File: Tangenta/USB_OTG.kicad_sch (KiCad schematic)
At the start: 21 parts, among them J11 TYPEC-304-ACP16, U10 TUSB321RWBR, U11 AOZ1353DI-01, U12 PUSB2X4Y-N, U9 PUSB2X4Y-N

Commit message: ...
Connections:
- net GNDREF: now also J11.A1B12 (GND), J11.B1A12 (GND); no longer J11.A1_B12 (GND), J11.B1_A12 (GND)
- net USB_DR.VBUS: now also J11.A4B9 (VBUS), J11.B4A9 (VBUS); no longer J11.A4_B9 (VBUS), J11.B4_A9 (VBUS)
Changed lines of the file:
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@@
     (stroke (width 0) (type default))
   )
-  (wire (pts (xy 102.108 142.494) (xy 86.36 142.494))
+  (wire (pts (xy 99.568 142.494) (xy 83.82 142.494))
     (stroke (width 0) (type default))
   )
@@
     (stroke (width 0) (type default))
   )
-  (wire (pts (xy 124.968 150.114) (xy 140.716 150.114))
+  (wire (pts (xy 127.508 150.114) (xy 143.256 150.114))
     (stroke (width 0) (type default))
   )
@@
     (stroke (width 0) (type default))
   )
-  (wire (pts (xy 102.108 145.034) (xy 86.36 145.034))
+  (wire (pts (xy 99.568 145.034) (xy 83.82 145.034))
     (stroke (width 0) (type default))
   )
@@
     (stroke (width 0) (type default))
   )
-  (wire (pts (xy 124.968 152.654) (xy 140.716 152.654))
+  (wire (pts (xy 127.508 152.654) (xy 143.256 152.654))
     (stroke (width 0) (type default))
   )
@@
     (stroke (width 0) (type default))
   )
-  (wire (pts (xy 102.108 152.654) (xy 86.36 152.654))
+  (wire (pts (xy 99.568 152.654) (xy 83.82 152.654))
     (stroke (width 0) (type default))
   )
@@
     (stroke (width 0) (type default))
   )
-  (wire (pts (xy 124.968 139.954) (xy 140.716 139.954))
+  (wire (pts (xy 127.508 139.954) (xy 143.256 139.954))
     (stroke (width 0) (type default))
   )
@@
     (stroke (width 0) (type default))
   )
-  (wire (pts (xy 124.968 145.034) (xy 140.716 145.034))
+  (wire (pts (xy 127.508 145.034) (xy 143.256 145.034))
     (stroke (width 0) (type default))
   )
@@
     (stroke (width 0) (type default))
   )
-  (wire (pts (xy 86.36 150.114) (xy 102.108 150.114))
+  (wire (pts (xy 83.82 150.114) (xy 99.568 150.114))
     (stroke (width 0) (type default))
   )
@@
     (stroke (width 0) (type default))
   )
-  (wire (pts (xy 102.108 147.574) (xy 86.36 147.574))
+  (wire (pts (xy 99.568 147.574) (xy 83.82 147.574))
     (stroke (width 0) (type default))
   )
@@
     (stroke (width 0) (type default))
   )
-  (wire (pts (xy 124.968 147.574) (xy 140.716 147.574))
+  (wire (pts (xy 127.508 147.574) (xy 143.256 147.574))
     (stroke (width 0) (type default))
   )
@@
     (effects (font (size 1.27 1.27)) (justify right bottom))
   )
-  (label "USB_DR.P" (at 86.36 145.034 0) (fields_autoplaced)
+  (label "USB_DR.P" (at 83.82 145.034 0) (fields_autoplaced)
     (effects (font (size 1.27 1.27)) (justify left bottom))
   )
@@
     (effects (font (size 1.27 1.27)) (justify left bottom))
   )
-  (label "USB_DR.N" (at 86.36 142.494 0) (fields_autoplaced)
+  (label "USB_DR.N" (at 83.82 142.494 0) (fields_autoplaced)
     (effects (font (size 1.27 1.27)) (justify left bottom))
   )
@@
     (effects (font (size 1.27 1.27)) (justify left bottom))
   )
-  (label "USB_DR.N" (at 140.716 145.034 180) (fields_autoplaced)
-    (effects (font (size 1.27 1.27)) (justify right bottom))
-  )
-  (label "GND" (at 86.36 152.654 0) (fields_autoplaced)
+  (label "USB_DR.N" (at 143.256 145.034 180) (fields_autoplaced)
+    (effects (font (size 1.27 1.27)) (justify right bottom))
+  )
+  (label "GND" (at 83.82 152.654 0) (fields_autoplaced)
     (effects (font (size 1.27 1.27)) (justify left bottom))
   )
@@
     (effects (font (size 1.27 1.27)) (justify left bottom))
   )
-  (label "USB_DR_CC2" (at 140.716 150.114 180) (fields_autoplaced)
+  (label "USB_DR_CC2" (at 143.256 150.114 180) (fields_autoplaced)
     (effects (font (size 1.27 1.27)) (justify right bottom))
   )
@@
     (effects (font (size 1.27 1.27)) (justify right bottom))
   )
-  (label "USB_DR.VBUS" (at 86.36 150.114 0) (fields_autoplaced)
+  (label "USB_DR.VBUS" (at 83.82 150.114 0) (fields_autoplaced)
     (effects (font (size 1.27 1.27)) (justify left bottom))
   )
@@
     (effects (font (size 1.27 1.27)) (justify right bottom))
   )
-  (label "USB_DR.VBUS" (at 140.716 139.954 180) (fields_autoplaced)
+  (label "USB_DR.VBUS" (at 143.256 139.954 180) (fields_autoplaced)
     (effects (font (size 1.27 1.27)) (justify right bottom))
   )
@@
     (effects (font (size 1.27 1.27)) (justify right bottom))
   )
-  (label "USB_DR_CC1" (at 86.36 147.574 0) (fields_autoplaced)
+  (label "USB_DR_CC1" (at 83.82 147.574 0) (fields_autoplaced)
     (effects (font (size 1.27 1.27)) (justify left bottom))
   )
@@
     (effects (font (size 1.27 1.27)) (justify right bottom))
   )
-  (label "GND" (at 140.716 152.654 180) (fields_autoplaced)
-    (effects (font (size 1.27 1.27)) (justify right bottom))
-  )
-  (label "USB_DR.P" (at 140.716 147.574 180) (fields_autoplaced)
+  (label "GND" (at 143.256 152.654 180) (fields_autoplaced)
+    (effects (font (size 1.27 1.27)) (justify right bottom))
+  )
+  (label "USB_DR.P" (at 143.256 147.574 180) (fields_autoplaced)
     (effects (font (size 1.27 1.27)) (justify right bottom))
   )
@@
     )
     (pin "13")
-    (pin "A1_B12")
-    (pin "A4_B9")
+    (pin "A1B12")
+    (pin "A4B9")
     (pin "A5")
     (pin "A6")
     (pin "A7")
     (pin "A8")
-    (pin "B1_A12")
-    (pin "B4_A9")
+    (pin "B1A12")
+    (pin "B4A9")
     (pin "B5")
     (pin "B6")

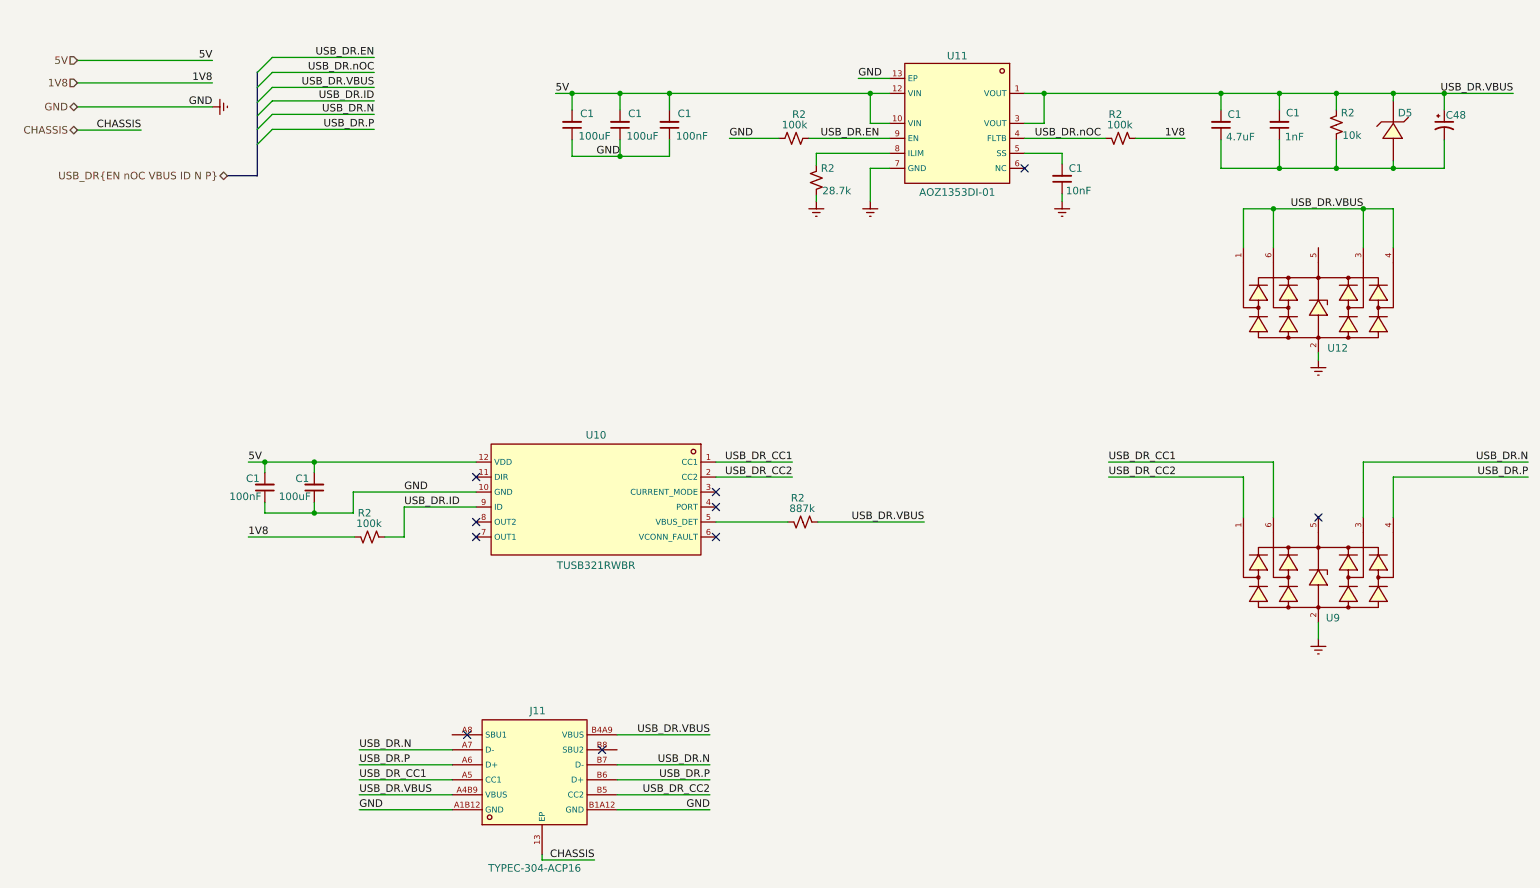
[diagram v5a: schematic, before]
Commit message: USB dual role routed.
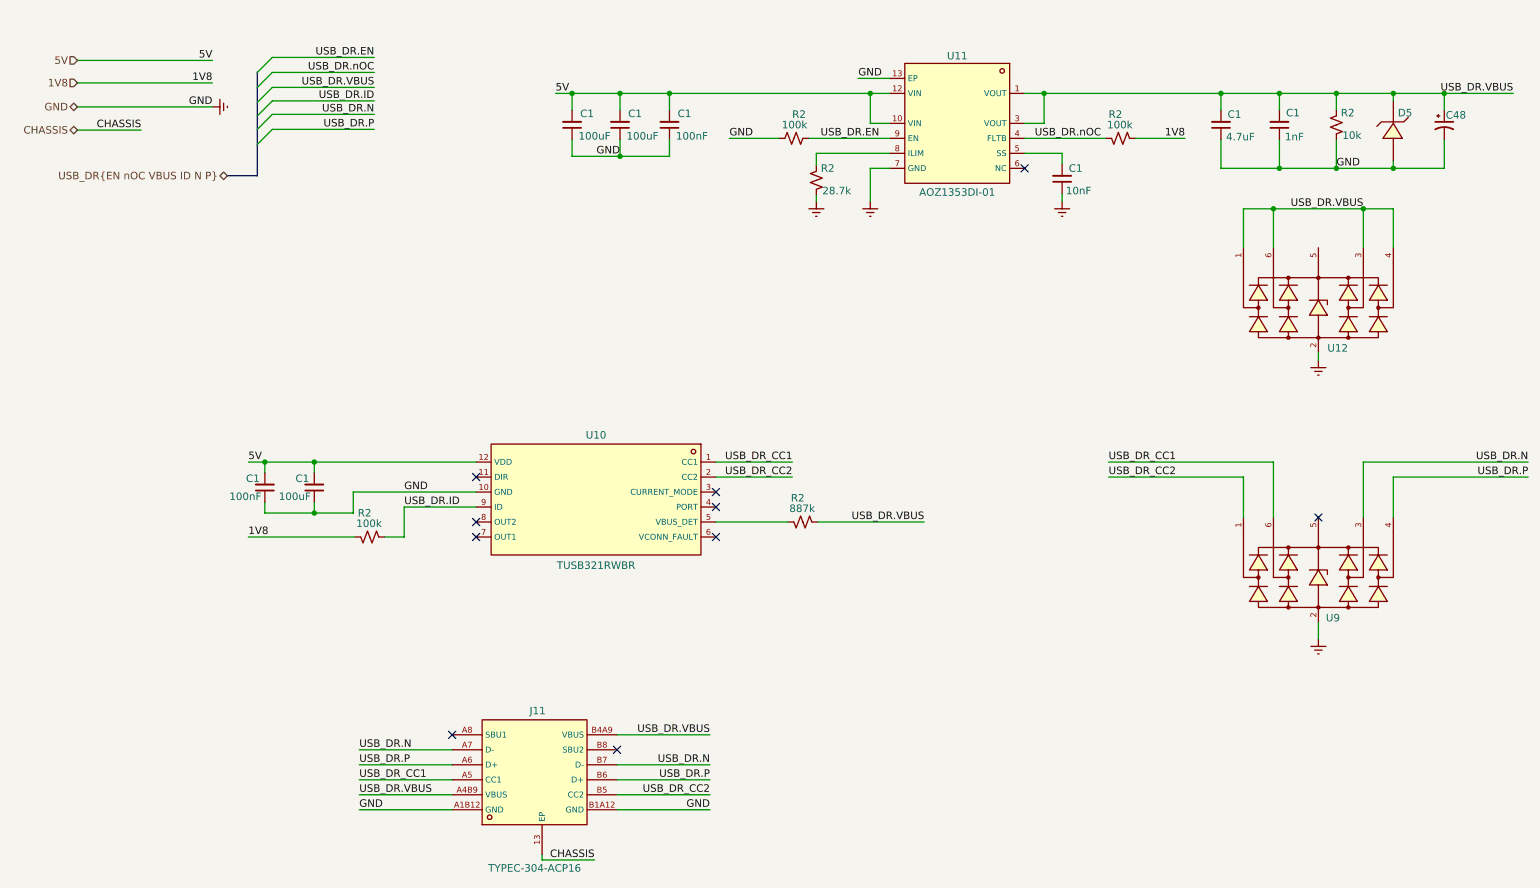
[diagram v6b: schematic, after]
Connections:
- net GNDREF: now also C1.1, C1.1, C48.2, D5.2 (A), R2.1
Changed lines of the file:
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@@
   )
   (no_connect (at 144.272 101.346))
-  (no_connect (at 124.968 142.494))
+  (no_connect (at 127.508 142.494))
   (no_connect (at 103.632 103.886))
   (no_connect (at 144.272 106.426))
@@
   (no_connect (at 103.632 96.266))
   (no_connect (at 103.632 106.426))
-  (no_connect (at 102.108 139.954))
+  (no_connect (at 99.568 139.954))
   (no_connect (at 144.272 98.806))
   (bus_entry (at 66.548 37.338) (size 2.54 -2.54)
@@
     (stroke (width 0) (type default))
   )
+  (label "GND" (at 249.428 43.942 0) (fields_autoplaced)
+    (effects (font (size 1.27 1.27)) (justify left bottom))
+  )
   (label "1V8" (at 65.024 106.426 0) (fields_autoplaced)
